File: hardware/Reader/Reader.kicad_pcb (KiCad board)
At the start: 4 copper layers, 66.7 x 104.8 mm, 138 parts, among them CN1 AHDF15A-KG-TAXB

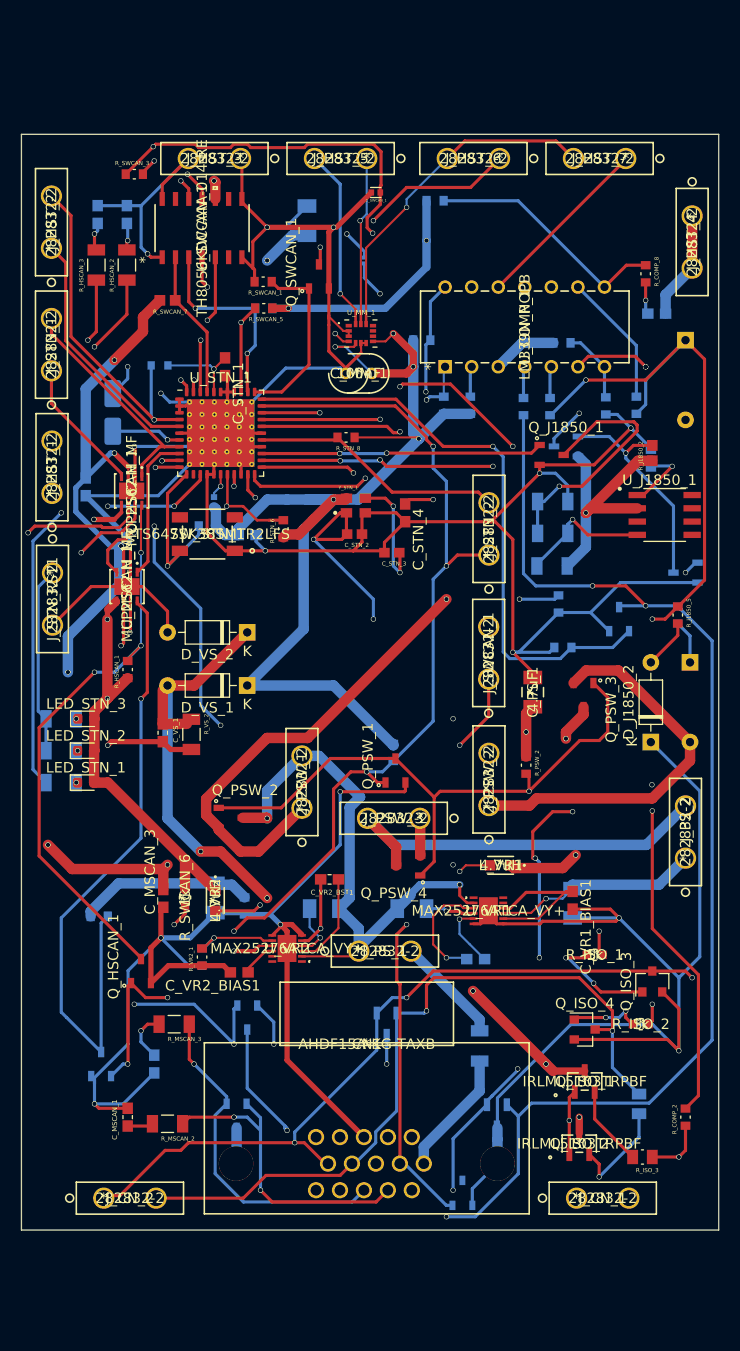
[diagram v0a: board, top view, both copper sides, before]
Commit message: Fixed bugs in schematic. Updated BOM list. Swapped to using ESP32 holder. Updated PCB layout to v0.0.2. Updated schematic to v0.0.4
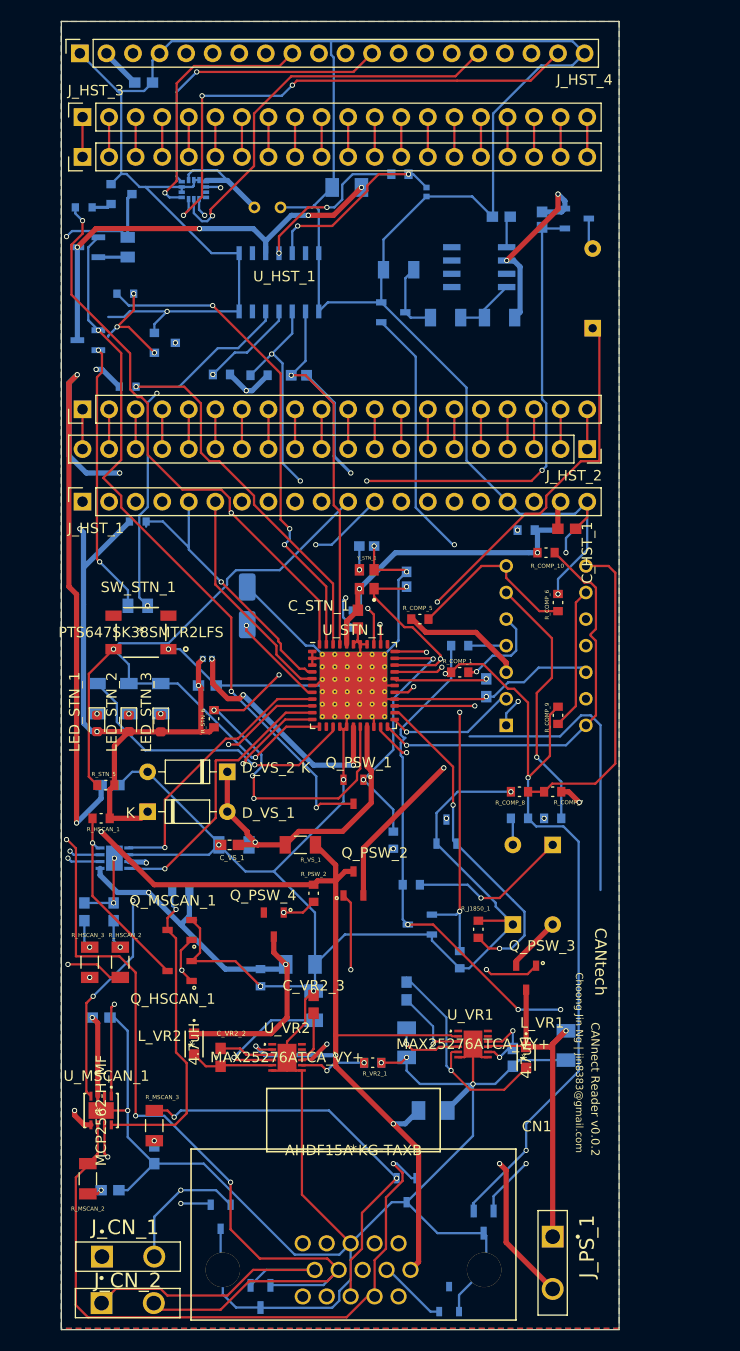
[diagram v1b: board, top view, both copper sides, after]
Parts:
- removed J_HST_5, J_HST_6, J_HST_7, J_PSW_1, J_PSW_2, J_PSW_3, J_PS_2, J_STN_1, J_STN_2, J_STN_RST1, J_SWCAN_1: 282832-2, footprints:282832-2
- removed Q_SWCAN_1: NX7002AK,215, footprints:SOT95P230X110-3N
- removed R_SWCAN_1: 10k, footprints:RESC1608X55N
- removed R_SWCAN_2: 130, footprints:RESC0603X26N
- added C_HST_2: 1uF, footprints:0603, B.Cu at (120.9, 49.0)
- added U_HST_1: ESP32_Holder, footprints:ESP32_Holder, F.Cu at (140.5, 67.6)
- C_HST_1, Q_MSCAN_1, R_COMP_1, R_COMP_10, R_COMP_5, R_COMP_6, R_COMP_7, R_COMP_9, R_J1850_1, R_STN_5, R_VS_1: moved to F.Cu
- C_MM_1, C_MSCAN_1, C_MSCAN_3, C_PS_1, C_STN_2, C_STN_3, C_STN_4, C_SWCAN_1, D_J1850_2, Q_ISO_1, Q_ISO_2, Q_ISO_3, Q_ISO_4, Q_J1850_1, R_COMP_2, R_ISO_1, R_ISO_2, R_ISO_3, R_J1850_2, R_J1850_5, R_STN_8, R_SWCAN_3, R_SWCAN_5, R_SWCAN_6, R_SWCAN_7, R_VS_2, U_COMP_1, U_HSCAN_1, U_J1850_1, U_MM_1, U_SWCAN_1: moved to B.Cu
- C_VR1_3: renamed from C_VR1_BIAS1; moved to B.Cu
- J_CN_1, J_CN_2, J_PS_1: value 282832-2 -> 1546931-2; footprint footprints:282832-2 -> footprints:1546931-2
- J_HST_1, J_HST_2, J_HST_3, J_HST_4: value 282832-2 -> 4157; footprint footprints:282832-2 -> Connector_PinSocket_2.54mm:PinSocket_1x20_P2.54mm_Vertical
- moved Q_ISO_2 97.8 mm to (115.6, 64.8), turned to 270 degrees
- moved R_ISO_4 95.4 mm to (119.4, 64.8)
- moved R_ISO_2 94.5 mm to (115.2, 61.0), turned to 180 degrees
- moved Q_ISO_4 91.3 mm to (118.8, 59.7)
- moved Q_ISO_1 85.3 mm to (115.6, 73.7), turned to 270 degrees
- moved R_ISO_1 77.5 mm to (119.2, 69.2), turned to 180 degrees
- moved Q_ISO_3 76.8 mm to (122.9, 73.9), turned to 0 degrees
- moved R_ISO_3 71.5 mm to (120.3, 99.1)
- moved C_HSCAN_1 66.7 mm to (118.0, 128.3)
- moved C_HSCAN_2 66.7 mm to (115.2, 128.3)
- moved R_HSCAN_2 66.7 mm to (118.7, 133.1)
- moved R_HSCAN_3 66.7 mm to (115.7, 133.1)
- moved J_HST_4 60.6 mm to (114.8, 46.2), turned to 90 degrees
- moved R_COMP_7 57.6 mm to (160.0, 116.8), turned to 180 degrees
- moved J_HST_2 54.7 mm to (163.3, 84.1), turned to 270 degrees
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- renumbered C_VR1_in1 to C_VR1_1, C_VR1_BST1 to C_VR1_2, C_VR2_in1 to C_VR2_1, C_VR2_BST1 to C_VR2_2, C_VR2_BIAS1 to C_VR2_3
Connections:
- C_PS_1 pad 1: +12V -> Pin16_Raw_+12V_Battery
- C_SWCAN_2 pad 1: +12V -> Pin16_Raw_+12V_Battery
- C_VR1_1 pad 1: Net-(C_VR1_in1-Pad1) -> Pin4_GnD_Chassis
- C_VR1_1 pad 2: +12V -> Net-(C_VR1_1-Pad2)
- C_VR2_1 pad 2: +12V -> Pin4_GnD_Chassis
- C_VS_1 pad 1: /OBDII Interpreter/Analog_Voltage -> /Host/Analog_Voltage
- D_VS_1 pad 2: /OBDII Interpreter/Analog_Voltage -> /Host/Analog_Voltage
- D_VS_2 pad 1: /OBDII Interpreter/Analog_Voltage -> /Host/Analog_Voltage
- J_HST_1 pad 1: /OBDII Interpreter/~RESET_OBD_HW~ -> /Host/Analog_Voltage
- J_HST_1 pad 2: /OBDII Interpreter/RESET_OBD_SW -> Net-(J_HST_1-Pad2)
- J_HST_2 pad 1: /Host/HOST_RX -> Net-(J_HST_2-Pad1)
- J_HST_2 pad 2: /Host/HOST_TX -> Net-(J_HST_2-Pad2)
- J_HST_3 pad 1: Pin4_GnD_Chassis -> Net-(J_HST_3-Pad1)
- J_HST_3 pad 2: Pin4_GnD_Chassis -> Net-(J_HST_3-Pad2)
- J_HST_4 pad 1: +5V -> Pin4_GnD_Chassis
- J_PS_1 pad 1: +12V -> +5V
- J_PS_1 pad 2: /OBDII Interpreter/Analog_Voltage -> +3V3
- Q_HSCAN_1 pad 1: /OBDII Interpreter/~PWR_CTRL~ -> /Host/~PWR_CTRL~
- Q_ISO_1 pad 3: +12V -> Pin16_Raw_+12V_Battery
- Q_ISO_2 pad 3: +12V -> Pin16_Raw_+12V_Battery
- Q_MSCAN_1 pad 1: /OBDII Interpreter/~PWR_CTRL~ -> /Host/~PWR_CTRL~
- Q_PSW_1 pad 1: /OBDII Interpreter/~PWR_CTRL~ -> /Host/~PWR_CTRL~
- Q_PSW_2 pad 3: +12V -> Pin16_Raw_+12V_Battery
- R_PSW_1 pad 2: /OBDII Interpreter/~PWR_CTRL~ -> /Host/~PWR_CTRL~
- R_PSW_2 pad 1: +12V -> Pin16_Raw_+12V_Battery
- R_VS_1 pad 2: /OBDII Interpreter/Analog_Voltage -> /Host/Analog_Voltage
- R_VS_2 pad 1: /OBDII Interpreter/Analog_Voltage -> /Host/Analog_Voltage
- U_MM_1 pad 4: /Host/MEMS_INT -> /Host/MEMS_INT1
- U_MM_1 pad 9: /Reader MEMs/MEMS_INT2 -> /Host/MEMS_INT2
- U_STN_1 pad 19: /OBDII Interpreter/Analog_Voltage -> /Host/Analog_Voltage
- U_STN_1 pad 32: /OBDII Interpreter/~PWR_CTRL~ -> /Host/~PWR_CTRL~
- U_SWCAN_1 pad 10: +12V -> Pin16_Raw_+12V_Battery
- U_VR1 pad 2: +12V -> Pin16_Raw_+12V_Battery
- U_VR1 pad 4: Net-(C_VR1_in1-Pad1) -> Net-(C_VR1_1-Pad2)
- U_VR2 pad 2: +12V -> Pin16_Raw_+12V_Battery
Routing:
- net +12V: track 186.8 -> 0.00 mm, vias 9 -> 0
- net Pin16_Raw_+12V_Battery: track 12.0 -> 194.3 mm, vias 0 -> 8
- net /OBDII Interpreter/~PWR_CTRL~: track 105.9 -> 0.00 mm, vias 6 -> 0
- net /OBDII Interpreter/Analog_Voltage: track 84.0 -> 0.00 mm, vias 3 -> 0
- net Pin15_ISO9141_L-Line: track 71.9 -> 154.8 mm, vias 2 -> 4
- net Pin6_ISO15765_CAN_BUS_High: track 139.6 -> 67.3 mm, vias 4 -> 3
- net /Host/~PWR_CTRL~: track 0.00 -> 72.2 mm, vias 0 -> 3
- net /Host/Analog_Voltage: track 0.00 -> 70.5 mm, vias 0 -> 1
- net Pin7_ISO9141_K-Line: track 96.4 -> 164.0 mm
- net Pin14_ISO15765_CAN_BUS_Low: track 153.2 -> 87.7 mm
- net Pin4_GnD_Chassis: track 722.4 -> 659.4 mm, vias 21 -> 18
- net Net-(R_COMP_2-Pad2): track 84.9 -> 25.0 mm, vias 4 -> 1
- net Net-(Q_J1850_2-Pad3): track 21.4 -> 79.6 mm, vias 1 -> 3
- net Net-(J_SWCAN_1-Pad2): track 44.8 -> 0.00 mm, vias 3 -> 0
- net Net-(C_STN_2-Pad2): track 62.1 -> 17.7 mm, vias 3 -> 2
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- added copper zone on In2.Cu, net +3V3
- added copper zone on In1.Cu, net +5V
- added copper zone on B.Cu, net Pin4_GnD_Chassis
- added copper zone on F.Cu, net Pin4_GnD_Chassis
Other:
- board size 66.7 x 104.8 mm -> 53.3 x 125.1 mm
- net class Default: trace_width 0.25 -> 0.22; via_drill 0.4 -> 0.32
- net class Power: trace_width 0.7 -> 0.5; via_drill 0.4 -> 0.32
- rule via_min_size: 0.2 -> 0.5
- board text added: "CANnect Reader v0.0.2"
- board text added: "CANtech"
- board text added: "Choong Jin Ng | jin8383@gmail.com"
- board text removed: "CANtech | CANnect Reader v0.0.1"

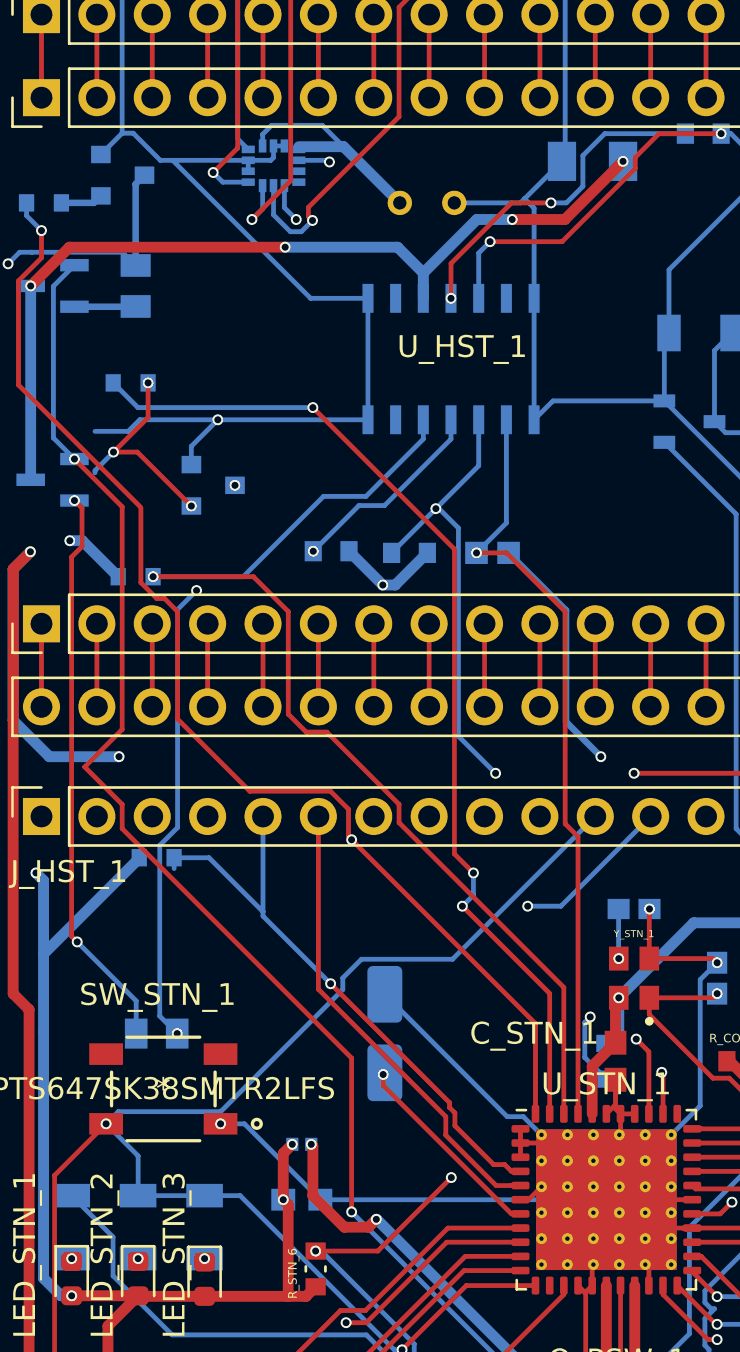
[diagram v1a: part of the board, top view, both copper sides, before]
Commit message: Fixed positions of components. Fixed silkscreen titles of components
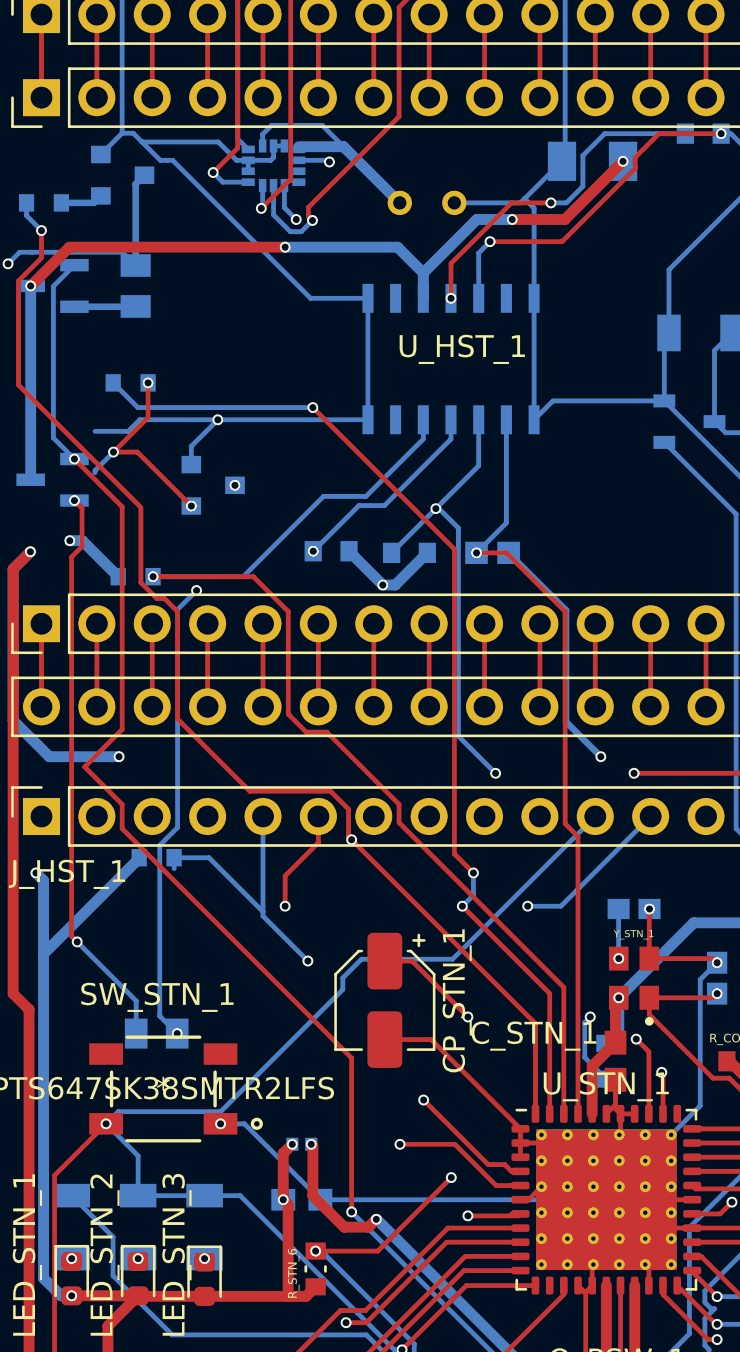
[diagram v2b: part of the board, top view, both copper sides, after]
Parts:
- CP_STN_1: moved to F.Cu
- moved CP_STN_1 1.52 mm to (130.8, 97.5), turned to 270 degrees
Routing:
- net Net-(CP_STN_1-Pad1): track 9.24 -> 16.9 mm, vias 1 -> 2
- net Pin4_GnD_Chassis: track 659.4 -> 655.0 mm
- net /Host/HOST_RX: track 22.2 -> 24.9 mm, vias 0 -> 2
- net /Host/I2C_SDA: track 49.6 -> 48.4 mm
- net /Host/HOST_TX: track 27.3 -> 27.5 mm, vias 1 -> 2

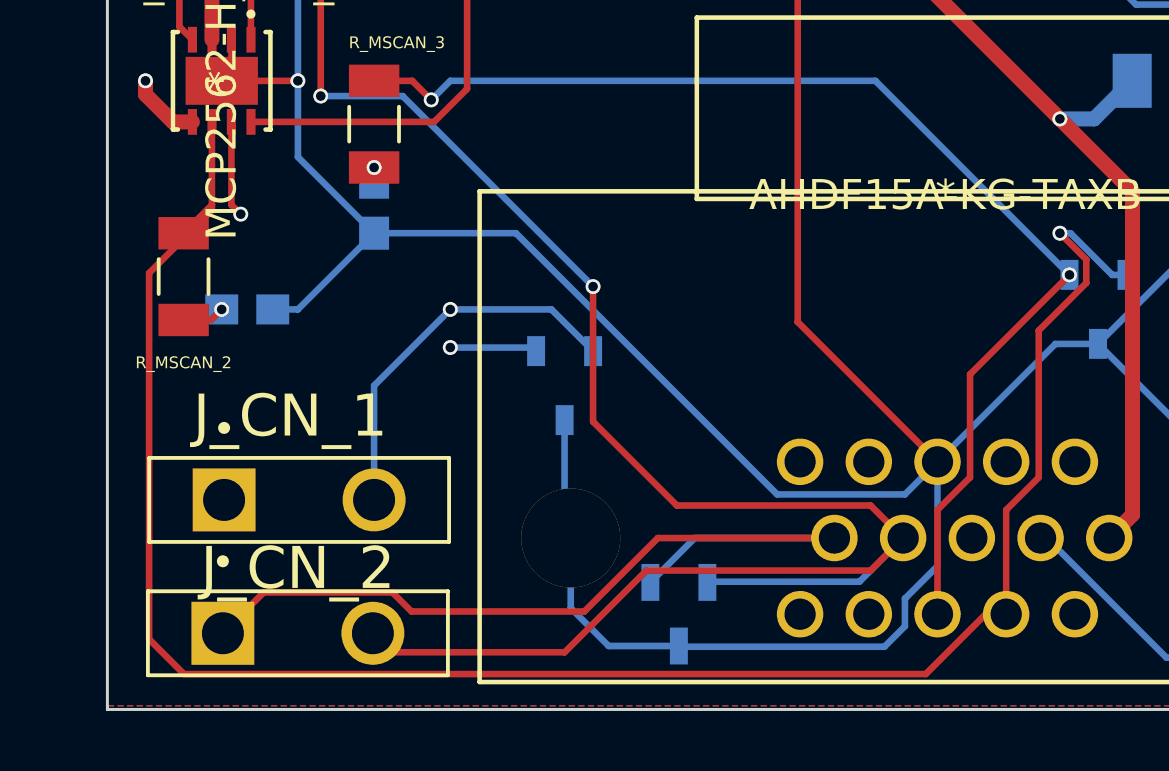
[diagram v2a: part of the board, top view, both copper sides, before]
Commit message: Made minor adjustments to PCB layout
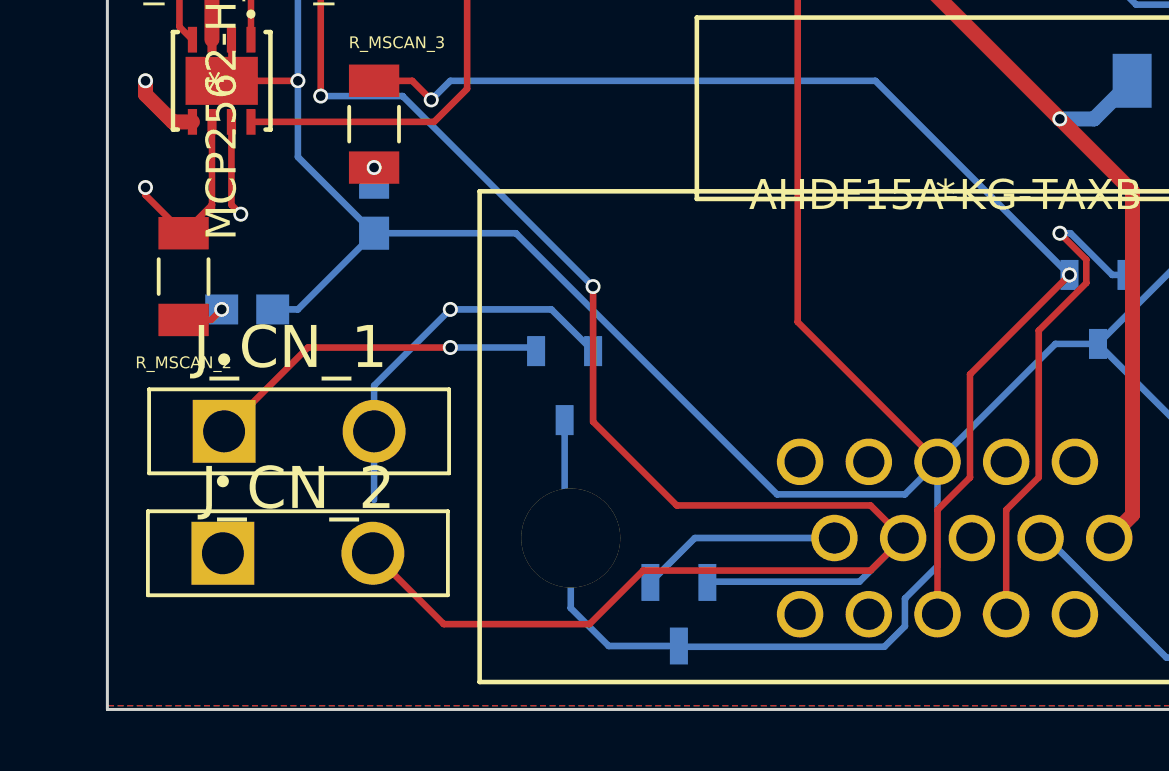
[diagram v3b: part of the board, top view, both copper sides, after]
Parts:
- moved J_CN_2 2.67 mm to (119.4, 163.1)
- moved J_CN_1 2.29 mm to (119.4, 159.0)
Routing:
- net Pin11_MS_CAN_Low: track 66.3 -> 60.6 mm, vias 1 -> 2
- net Pin6_ISO15765_CAN_BUS_High: track 67.3 -> 68.9 mm
